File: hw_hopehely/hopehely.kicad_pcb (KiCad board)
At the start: 2 copper layers, 48.3 x 55.8 mm, 39 parts, among them J1 Conn_2Rows-05Pins, Q1 AO3401A, Q2 AO3401A, Q3 AO3401A, SW1 SW_DPST_x2, T1 Tab, U1 PY32F002AF15P6TU

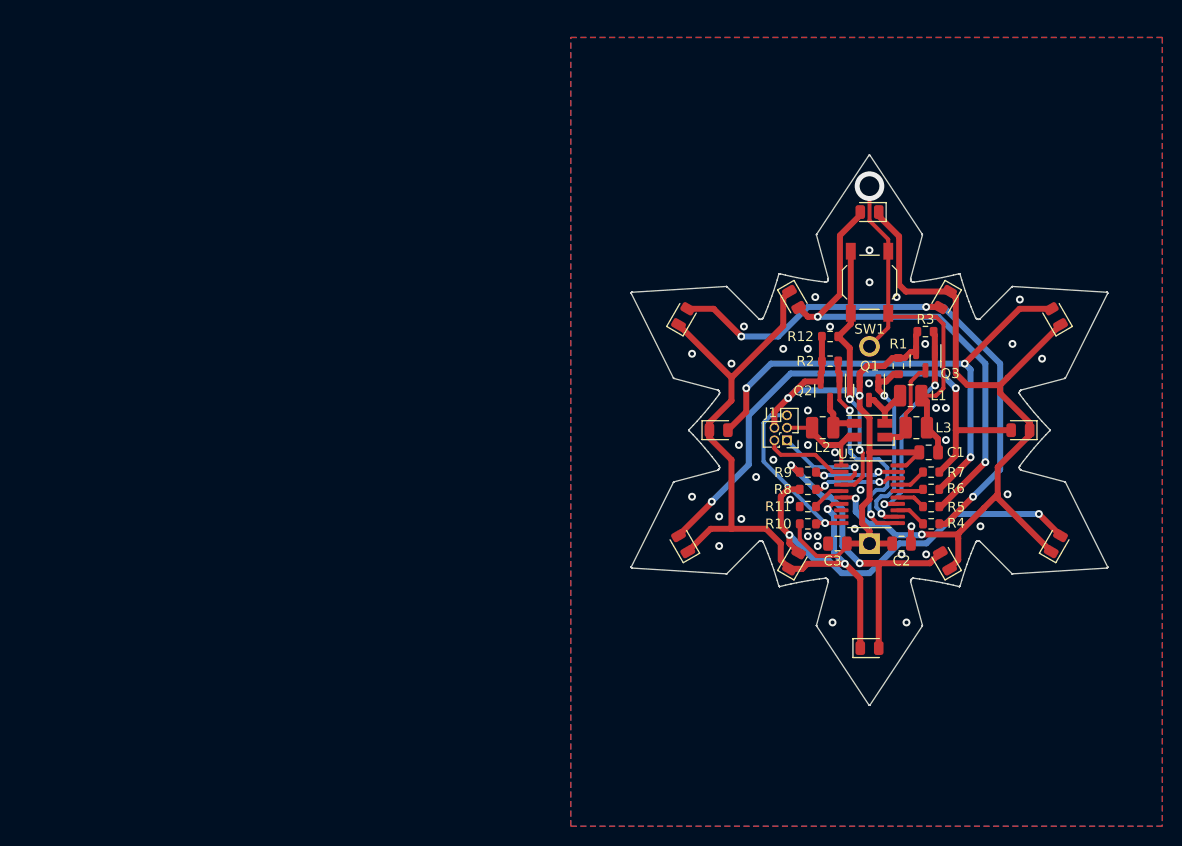
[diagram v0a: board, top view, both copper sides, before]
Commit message: Hoember + Mezi routed
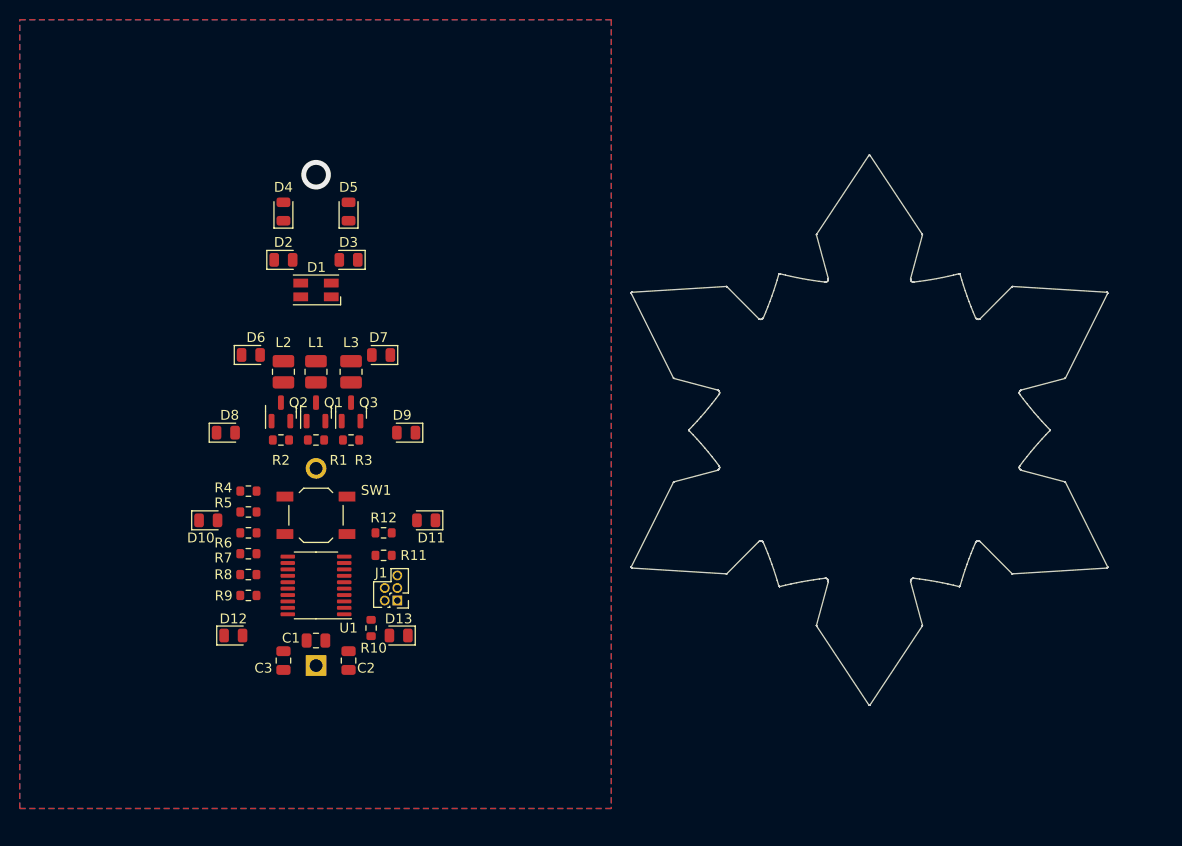
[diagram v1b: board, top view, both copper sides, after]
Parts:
- added T1: Tab, kikit:Tab, F.Cu at (111.8, 71.6)
- added T1: Tab, kikit:Tab, F.Cu at (130.2, 99.6)
- added T1: Tab, kikit:Tab, F.Cu at (130.0, 41.9)
- Q1, Q2, Q3: footprint karifa:SOT-23 -> sajat:SOT-23
- moved R7 69.7 mm to (123.2, 84.2), turned to 0 degrees
- moved R6 69.4 mm to (123.2, 82.0), turned to 0 degrees
- moved R4 69.3 mm to (123.2, 77.8), turned to 0 degrees
- moved R5 69.2 mm to (123.2, 79.9), turned to 0 degrees
- moved D7 68.5 mm to (136.7, 64.0), turned to 180 degrees
- moved C1 65.0 mm to (130.0, 93.0)
- moved D12 64.5 mm to (121.7, 92.5)
- moved D11 63.9 mm to (141.2, 80.8), turned to 180 degrees
- moved T1 63.1 mm to (147.3, 71.6)
- moved D9 62.3 mm to (139.2, 71.9)
- moved SW1 60.9 mm to (130.0, 80.3), turned to 180 degrees
- moved D3 60.6 mm to (133.3, 54.4), turned to 180 degrees
- moved L1 60.4 mm to (130.0, 65.7), turned to 90 degrees
- moved D10 59.6 mm to (119.1, 80.8), turned to 0 degrees
- moved R1 59.5 mm to (130.0, 72.6), turned to 180 degrees
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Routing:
- net /MPX1: track 81.4 -> 0.00 mm, vias 2 -> 0
- net /MPX2: track 72.8 -> 0.00 mm, vias 2 -> 0
- net VCC: track 67.1 -> 0.00 mm, vias 2 -> 0
- net Net-(D2-A): track 57.0 -> 0.00 mm, vias 3 -> 0
- net Net-(D6-A): track 53.6 -> 0.00 mm, vias 3 -> 0
- net Net-(D8-A): track 53.3 -> 0.00 mm, vias 2 -> 0
- net GND: track 51.4 -> 0.00 mm, vias 42 -> 1
- net Net-(D4-A): track 50.2 -> 0.00 mm, vias 2 -> 0
- net Net-(D10-A): track 41.2 -> 0.00 mm, vias 2 -> 0
- net Net-(D12-A): track 33.6 -> 0.00 mm, vias 2 -> 0
- net Net-(SW1A-A): track 26.9 -> 0.00 mm, vias 2 -> 0
- net /R: track 23.4 -> 0.00 mm, vias 2 -> 0
- net /G: track 21.3 -> 0.00 mm, vias 2 -> 0
- net /B: track 19.5 -> 0.00 mm, vias 2 -> 0
- net /nRST: track 18.0 -> 0.00 mm, vias 1 -> 0
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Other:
- board text added: "PCB by Dávid & Kristóf"
- board text removed: "PCB by Kristóf"

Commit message: Fixed remenyo's overwrite error.
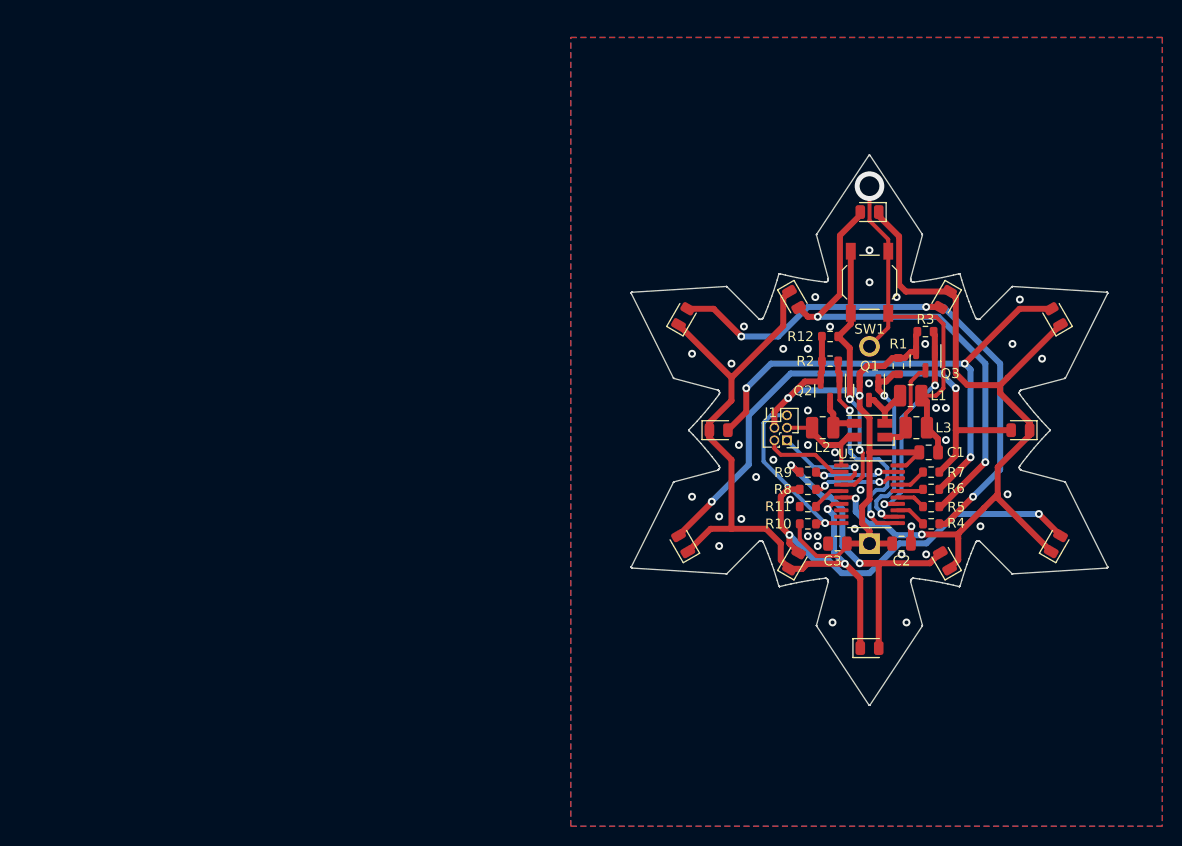
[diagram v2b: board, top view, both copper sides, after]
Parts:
- removed the T1 at (111.8, 71.6)
- removed the T1 at (130.2, 99.6)
- removed the T1 at (130.0, 41.9)
- Q1, Q2, Q3: footprint sajat:SOT-23 -> karifa:SOT-23
- moved R7 69.7 mm to (192.4, 75.9), turned to 180 degrees
- moved R6 69.4 mm to (192.4, 77.6), turned to 180 degrees
- moved R4 69.3 mm to (192.4, 81.1), turned to 180 degrees
- moved R5 69.2 mm to (192.4, 79.4), turned to 180 degrees
- moved D7 68.5 mm to (205.1, 60.1), turned to 120 degrees
- moved C1 65.0 mm to (192.2, 73.9)
- moved D12 64.5 mm to (186.2, 93.7)
- moved D11 63.9 mm to (205.1, 83.1), turned to 60 degrees
- moved T1 63.1 mm to (210.0, 79.0)
- moved D9 62.3 mm to (201.5, 71.6)
- moved SW1 60.9 mm to (186.2, 56.6), turned to 90 degrees
- moved D3 60.6 mm to (193.8, 58.4), turned to -120 degrees
- moved L1 60.4 mm to (190.4, 68.1), turned to 0 degrees
- moved D10 59.6 mm to (178.5, 84.9), turned to 60 degrees
- moved R1 59.5 mm to (189.1, 65.1), turned to -90 degrees
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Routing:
- net /MPX1: track 0.00 -> 81.4 mm, vias 0 -> 2
- net /MPX2: track 0.00 -> 72.8 mm, vias 0 -> 2
- net VCC: track 0.00 -> 67.1 mm, vias 0 -> 2
- net Net-(D2-A): track 0.00 -> 57.0 mm, vias 0 -> 3
- net Net-(D6-A): track 0.00 -> 53.6 mm, vias 0 -> 3
- net Net-(D8-A): track 0.00 -> 53.3 mm, vias 0 -> 2
- net GND: track 0.00 -> 51.4 mm, vias 1 -> 42
- net Net-(D4-A): track 0.00 -> 50.2 mm, vias 0 -> 2
- net Net-(D10-A): track 0.00 -> 41.2 mm, vias 0 -> 2
- net Net-(D12-A): track 0.00 -> 33.6 mm, vias 0 -> 2
- net Net-(SW1A-A): track 0.00 -> 26.9 mm, vias 0 -> 2
- net /R: track 0.00 -> 23.4 mm, vias 0 -> 2
- net /G: track 0.00 -> 21.3 mm, vias 0 -> 2
- net /B: track 0.00 -> 19.5 mm, vias 0 -> 2
- net /nRST: track 0.00 -> 18.0 mm, vias 0 -> 1
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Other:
- board text added: "PCB by Kristóf"
- board text removed: "PCB by Dávid & Kristóf"
